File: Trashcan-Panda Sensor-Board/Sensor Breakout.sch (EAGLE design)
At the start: 14 parts, among them J6 BM06B-SRSS-TBT(LF)(SN), U2 VL53L1X

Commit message: Rectangular Sensor Board
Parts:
- removed C1: 4.7uF, SparkFun-Capacitors:4.7UF0603
- removed JP3, JP4: STAND-OFF, SparkFun:STAND-OFF
- removed R1: 10k, SparkFun-Resistors:10KOHM-0603-1/10W-1%
- added C3: (no value), Custom Components:CAP-MF-10UF-1206
- added Q1: BSS215P, Custom Components:BSS215P
- added R4: 100k, Custom Components:RESISTOR-MF-100K-0805
- added U1: LIS3DH, Custom Components:LIS3DH
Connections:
- removed net !INT: J6.5, R1.1, U2.!INT
- new net !EN: J6.6, Q1.GATE, R4.1
- new net INT: J6.5, U1.INT1
- new net VCC-IN: J6.2, Q1.SOURCE, R4.2
- net !SHUT: no longer J6.6
- net GND: now also C3.P$2, U1.GND, U1.GND1; no longer C1.2
- net SCL: now also U1.SCL/SPC
- net SDA: now also U1.SDA/SDI/SDO
- net VCC: now also C3.P$1, Q1.DRAIN, U1.VDD, U1.VDD_IO; no longer C1.1, J6.2, R1.2

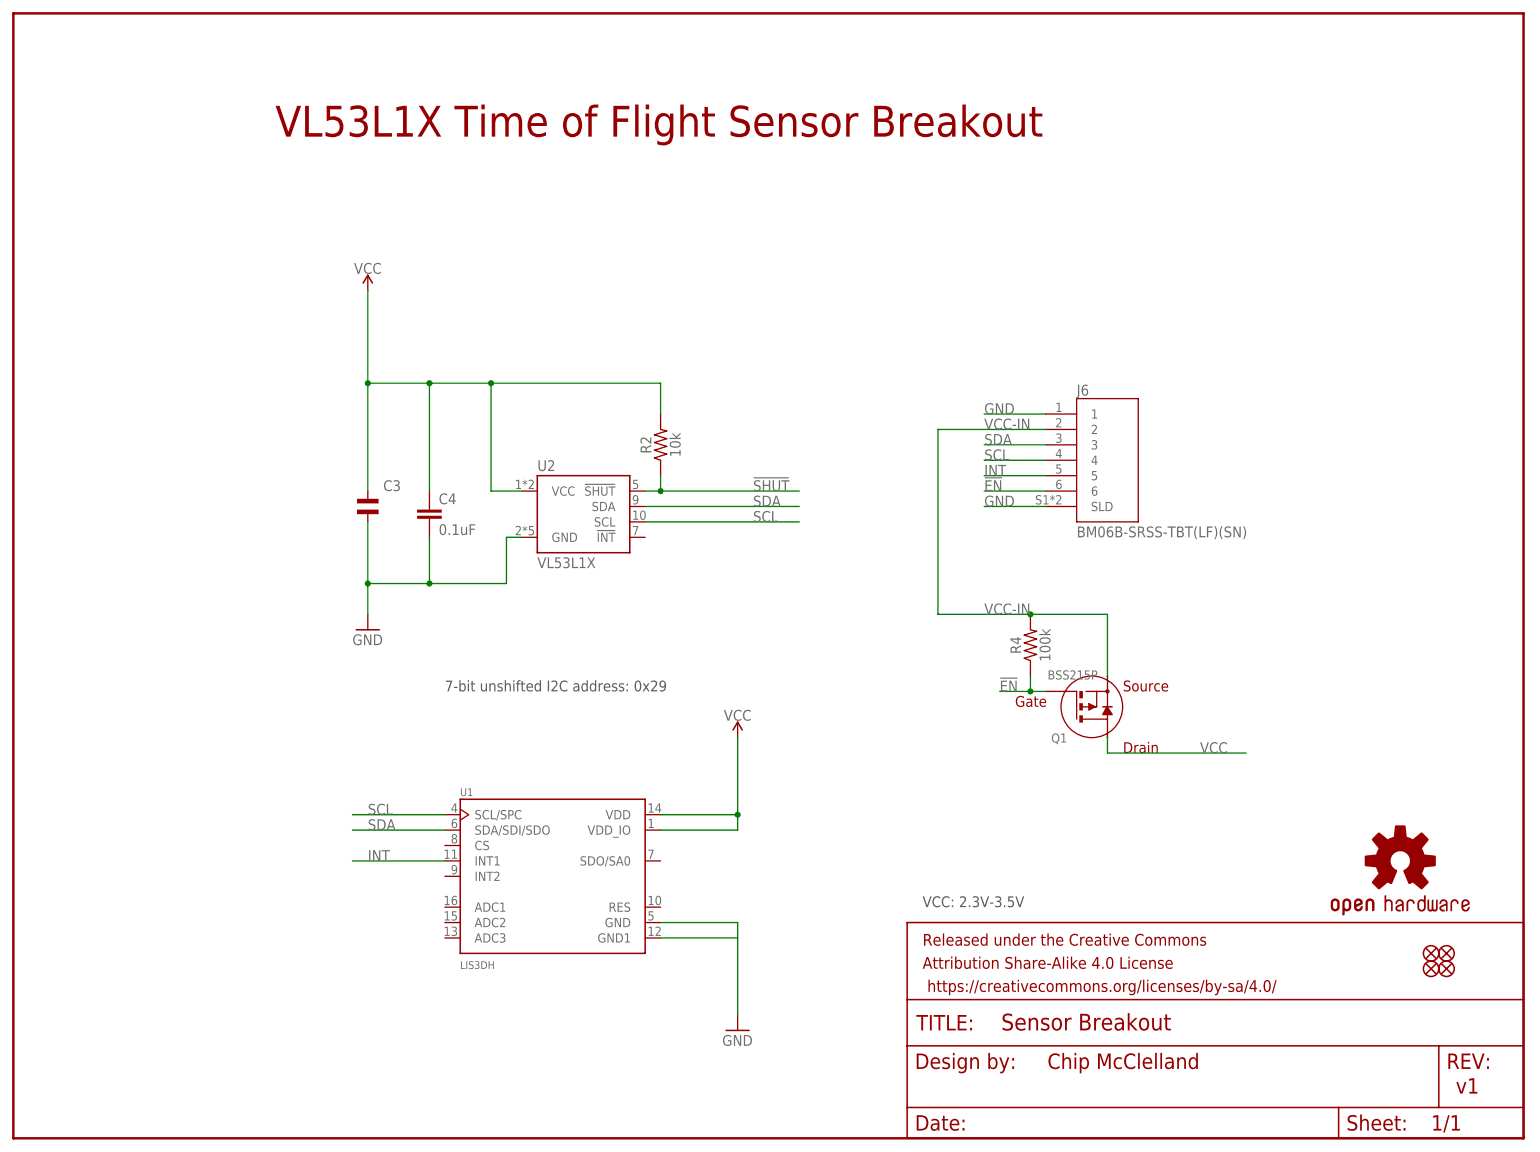
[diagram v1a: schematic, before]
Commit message: Updated battery board to v1.1
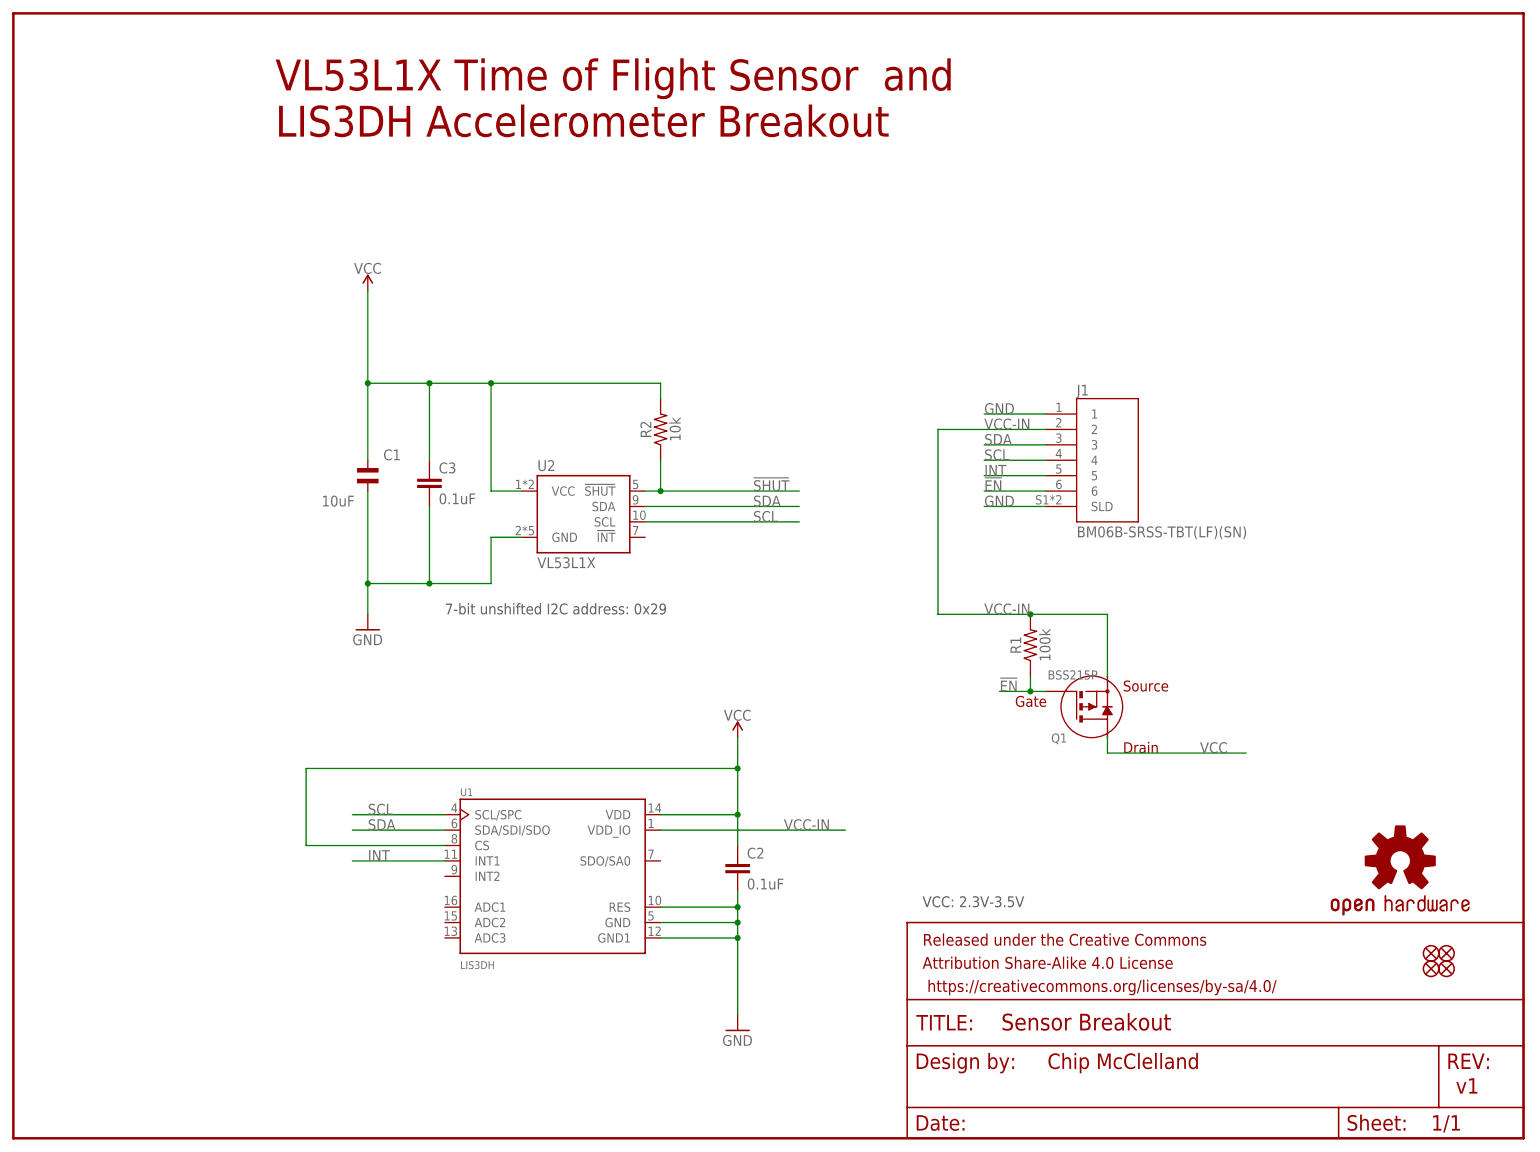
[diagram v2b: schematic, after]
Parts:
- removed C4: 0.1uF, SparkFun-Capacitors:0.1UF-0603-25V-(+80/-20%)
- added C1: 10uF, Custom Components:CAP-MF-10UF-1206
- added C2: 0.1uF, SparkFun-Capacitors:0.1UF-0603-25V-(+80/-20%)
- C3: value (none) -> 0.1uF; device Custom Components:CAP-MF-10UF-1206 -> SparkFun-Capacitors:0.1UF-0603-25V-(+80/-20%)
- renumbered J6 to J1, R4 to R1
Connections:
- net GND: now also C1.P$2, C2.2, C3.2, U1.RES; no longer C3.P$2, C4.2
- net VCC: now also C1.P$1, C2.1, C3.1, U1.CS; no longer C3.P$1, C4.1, U1.VDD_IO
- net VCC-IN: now also U1.VDD_IO
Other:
- note added: "VL53L1X Time of Flight Sensor and LIS3DH Accelerometer Breakout"
- note removed: "VL53L1X Time of Flight Sensor Breakout"
- moved on the sheet: R2

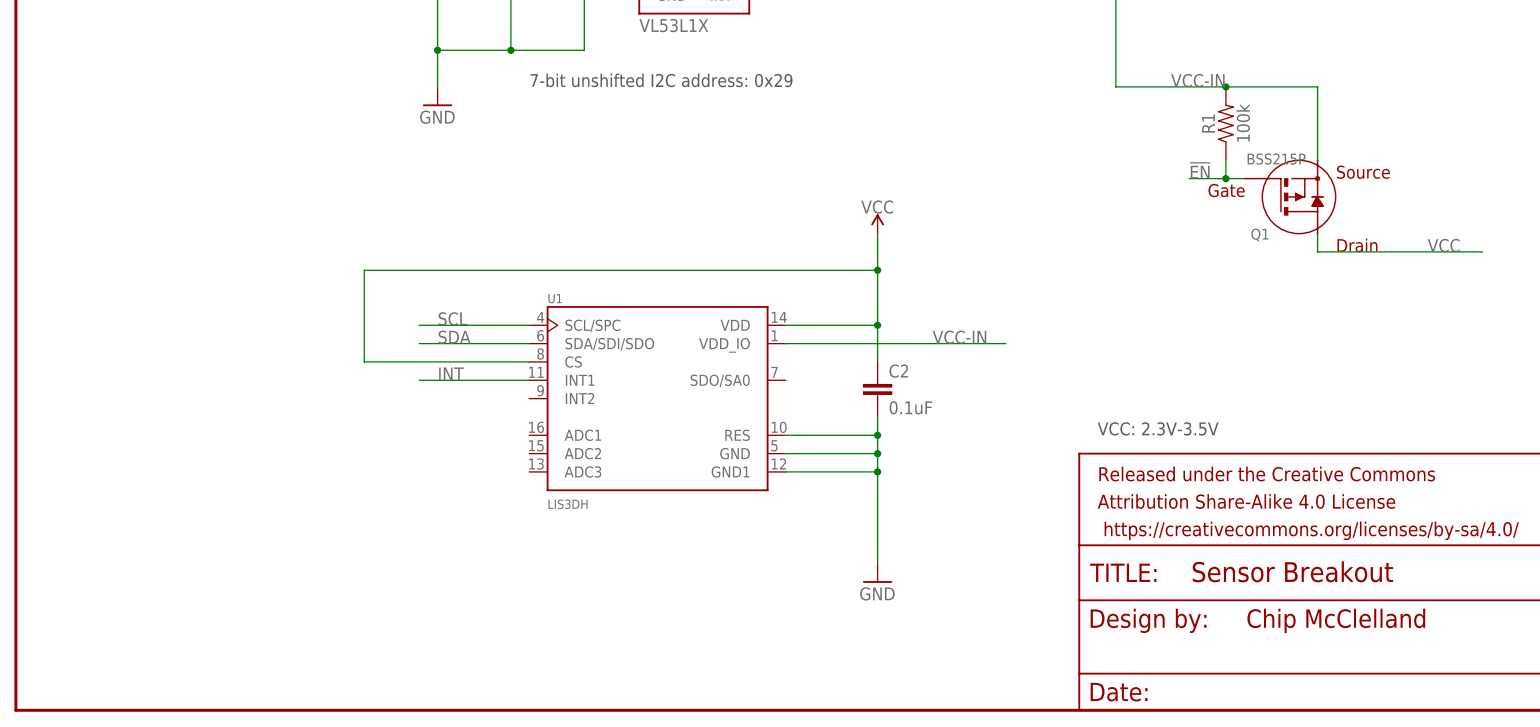
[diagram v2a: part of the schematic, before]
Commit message: Updated - Grounded address pin
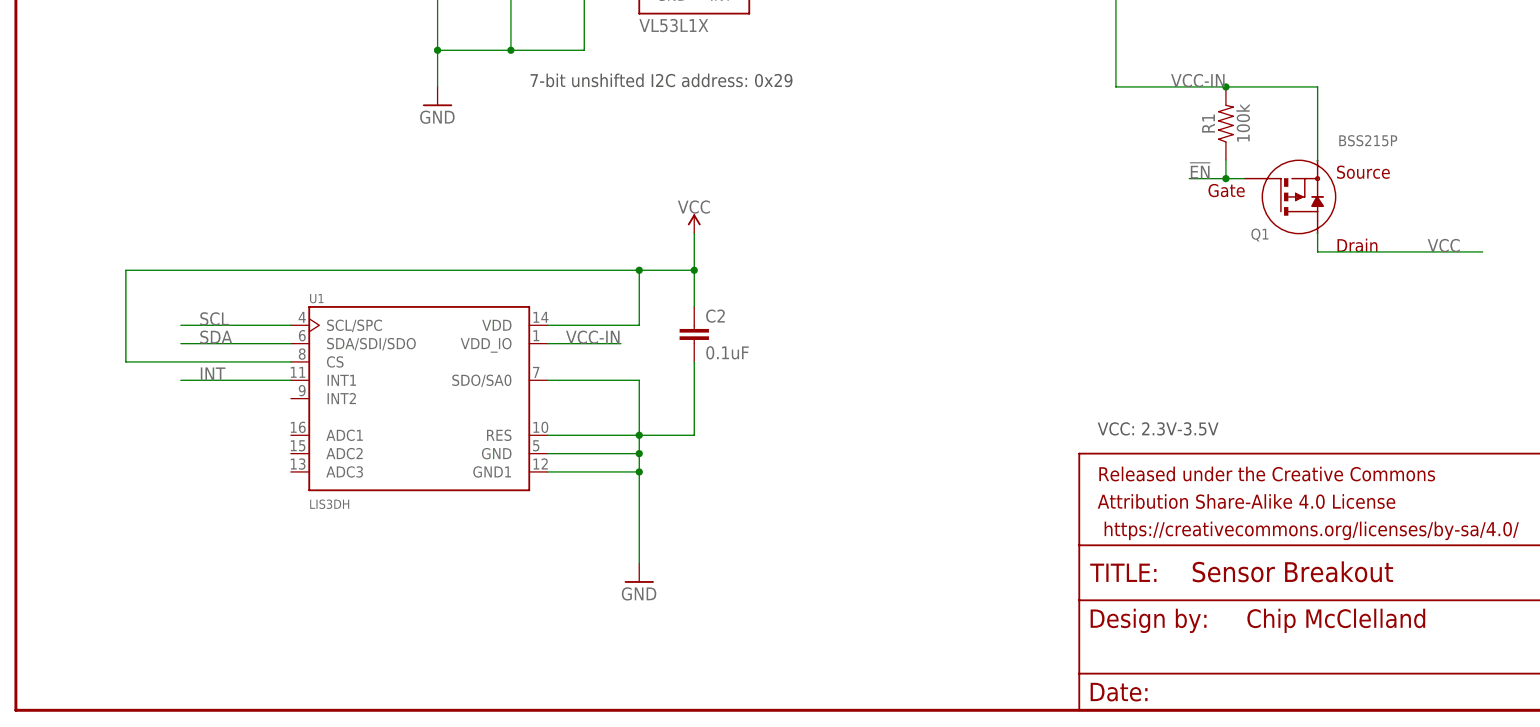
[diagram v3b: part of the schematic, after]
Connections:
- net GND: now also U1.SDO/SA0
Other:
- moved on the sheet: C2, U1
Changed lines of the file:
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@@
 <attribute name="VALUE" x="175.26" y="99.06" size="1.778" layer="96"/>
 </instance>
-<instance part="U1" gate="G$1" x="88.9" y="43.18" smashed="yes">
-<attribute name="NAME" x="73.6364" y="56.4085" size="1.27196875" layer="95"/>
-<attribute name="VALUE" x="73.6323" y="27.9123" size="1.272309375" layer="96"/>
-</instance>
-<instance part="SUPPLY1" gate="G$1" x="119.38" y="66.04" smashed="yes">
-<attribute name="VALUE" x="119.38" y="68.834" size="1.778" layer="96" align="bottom-center"/>
-</instance>
-<instance part="GND1" gate="1" x="119.38" y="17.78" smashed="yes">
-<attribute name="VALUE" x="116.84" y="15.24" size="1.778" layer="96"/>
+<instance part="U1" gate="G$1" x="55.88" y="43.18" smashed="yes">
+<attribute name="NAME" x="40.6164" y="56.4085" size="1.27196875" layer="95"/>
+<attribute name="VALUE" x="40.6123" y="27.9123" size="1.272309375" layer="96"/>
+</instance>
+<instance part="SUPPLY1" gate="G$1" x="93.98" y="66.04" smashed="yes">
+<attribute name="VALUE" x="93.98" y="68.834" size="1.778" layer="96" align="bottom-center"/>
+</instance>
+<instance part="GND1" gate="1" x="86.36" y="17.78" smashed="yes">
+<attribute name="VALUE" x="83.82" y="15.24" size="1.778" layer="96"/>
 </instance>
 <instance part="SUPPLY2" gate="G$1" x="58.42" y="139.7" smashed="yes">
@@
 </instance>
 <instance part="Q1" gate="G$1" x="177.8" y="71.12" smashed="yes">
-<attribute name="VALUE" x="170.46" y="77.12" size="1.5" layer="96" ratio="0" rot="MR180"/>
+<attribute name="VALUE" x="183.16" y="79.66" size="1.5" layer="96" ratio="0" rot="MR180"/>
 <attribute name="NAME" x="171.06" y="66.72" size="1.5" layer="95" ratio="0" rot="MR180"/>
 </instance>
-<instance part="C2" gate="G$1" x="119.38" y="43.18" smashed="yes">
-<attribute name="NAME" x="120.904" y="46.101" size="1.778" layer="95" font="vector"/>
-<attribute name="VALUE" x="120.904" y="41.021" size="1.778" layer="96" font="vector"/>
+<instance part="C2" gate="G$1" x="93.98" y="50.8" smashed="yes">
+<attribute name="NAME" x="95.504" y="53.721" size="1.778" layer="95" font="vector"/>
+<attribute name="VALUE" x="95.504" y="48.641" size="1.778" layer="96" font="vector"/>
 </instance>
 </instances>
@@
 <pinref part="GND1" gate="1" pin="GND"/>
 <pinref part="U1" gate="G$1" pin="GND"/>
-<wire x1="119.38" y1="35.56" x2="119.38" y2="33.02" width="0.1524" layer="91"/>
-<wire x1="119.38" y1="33.02" x2="119.38" y2="20.32" width="0.1524" layer="91"/>
-<wire x1="106.68" y1="35.56" x2="119.38" y2="35.56" width="0.1524" layer="91"/>
+<wire x1="86.36" y1="35.56" x2="86.36" y2="33.02" width="0.1524" layer="91"/>
+<wire x1="86.36" y1="33.02" x2="86.36" y2="20.32" width="0.1524" layer="91"/>
+<wire x1="73.66" y1="35.56" x2="86.36" y2="35.56" width="0.1524" layer="91"/>
 <pinref part="C2" gate="G$1" pin="2"/>
-<wire x1="119.38" y1="40.64" x2="119.38" y2="38.1" width="0.1524" layer="91"/>
-<junction x="119.38" y="35.56"/>
+<junction x="86.36" y="35.56"/>
 <pinref part="U1" gate="G$1" pin="RES"/>
-<wire x1="119.38" y1="38.1" x2="119.38" y2="35.56" width="0.1524" layer="91"/>
-<wire x1="106.68" y1="38.1" x2="119.38" y2="38.1" width="0.1524" layer="91"/>
-<junction x="119.38" y="38.1"/>
+<wire x1="86.36" y1="38.1" x2="86.36" y2="35.56" width="0.1524" layer="91"/>
+<wire x1="73.66" y1="38.1" x2="86.36" y2="38.1" width="0.1524" layer="91"/>
+<junction x="86.36" y="38.1"/>
 <pinref part="U1" gate="G$1" pin="GND1"/>
-<wire x1="106.68" y1="33.02" x2="119.38" y2="33.02" width="0.1524" layer="91"/>
-<junction x="119.38" y="33.02"/>
+<wire x1="73.66" y1="33.02" x2="86.36" y2="33.02" width="0.1524" layer="91"/>
+<junction x="86.36" y="33.02"/>
+<pinref part="U1" gate="G$1" pin="SDO/SA0"/>
+<wire x1="73.66" y1="45.72" x2="86.36" y2="45.72" width="0.1524" layer="91"/>
+<wire x1="86.36" y1="45.72" x2="86.36" y2="38.1" width="0.1524" layer="91"/>
+<wire x1="86.36" y1="38.1" x2="93.98" y2="38.1" width="0.1524" layer="91"/>
+<wire x1="93.98" y1="38.1" x2="93.98" y2="48.26" width="0.1524" layer="91"/>
 </segment>
 </net>
@@
 <segment>
 <pinref part="U1" gate="G$1" pin="SCL/SPC"/>
-<wire x1="71.12" y1="53.34" x2="55.88" y2="53.34" width="0.1524" layer="91"/>
-<label x="58.42" y="53.34" size="1.778" layer="95"/>
+<wire x1="38.1" y1="53.34" x2="22.86" y2="53.34" width="0.1524" layer="91"/>
+<label x="25.4" y="53.34" size="1.778" layer="95"/>
 </segment>
 </net>
@@
 <segment>
 <pinref part="U1" gate="G$1" pin="SDA/SDI/SDO"/>
-<wire x1="71.12" y1="50.8" x2="55.88" y2="50.8" width="0.1524" layer="91"/>
-<label x="58.42" y="50.8" size="1.778" layer="95"/>
+<wire x1="38.1" y1="50.8" x2="22.86" y2="50.8" width="0.1524" layer="91"/>
+<label x="25.4" y="50.8" size="1.778" layer="95"/>
 </segment>
 </net>
@@
 <pinref part="U1" gate="G$1" pin="VDD"/>
 <pinref part="SUPPLY1" gate="G$1" pin="VCC"/>
-<wire x1="106.68" y1="53.34" x2="119.38" y2="53.34" width="0.1524" layer="91"/>
-<wire x1="119.38" y1="53.34" x2="119.38" y2="60.96" width="0.1524" layer="91"/>
-<wire x1="119.38" y1="60.96" x2="119.38" y2="66.04" width="0.1524" layer="91"/>
-<junction x="119.38" y="53.34"/>
+<wire x1="73.66" y1="53.34" x2="86.36" y2="53.34" width="0.1524" layer="91"/>
+<wire x1="86.36" y1="53.34" x2="86.36" y2="60.96" width="0.1524" layer="91"/>
 <pinref part="C2" gate="G$1" pin="1"/>
-<wire x1="119.38" y1="48.26" x2="119.38" y2="53.34" width="0.1524" layer="91"/>
 <pinref part="U1" gate="G$1" pin="CS"/>
-<wire x1="71.12" y1="48.26" x2="48.26" y2="48.26" width="0.1524" layer="91"/>
-<wire x1="48.26" y1="48.26" x2="48.26" y2="60.96" width="0.1524" layer="91"/>
-<wire x1="48.26" y1="60.96" x2="119.38" y2="60.96" width="0.1524" layer="91"/>
-<junction x="119.38" y="60.96"/>
+<wire x1="38.1" y1="48.26" x2="15.24" y2="48.26" width="0.1524" layer="91"/>
+<wire x1="15.24" y1="48.26" x2="15.24" y2="60.96" width="0.1524" layer="91"/>
+<wire x1="15.24" y1="60.96" x2="86.36" y2="60.96" width="0.1524" layer="91"/>
+<junction x="86.36" y="60.96"/>
+<wire x1="86.36" y1="60.96" x2="93.98" y2="60.96" width="0.1524" layer="91"/>
+<wire x1="93.98" y1="60.96" x2="93.98" y2="55.88" width="0.1524" layer="91"/>
+<wire x1="93.98" y1="66.04" x2="93.98" y2="60.96" width="0.1524" layer="91"/>
+<junction x="93.98" y="60.96"/>
 </segment>
 <segment>
@@
 <segment>
 <pinref part="U1" gate="G$1" pin="INT1"/>
-<wire x1="71.12" y1="45.72" x2="55.88" y2="45.72" width="0.1524" layer="91"/>
-<label x="58.42" y="45.72" size="1.778" layer="95"/>
+<wire x1="38.1" y1="45.72" x2="22.86" y2="45.72" width="0.1524" layer="91"/>
+<label x="25.4" y="45.72" size="1.778" layer="95"/>
 </segment>
 <segment>
@@
 <segment>
 <pinref part="U1" gate="G$1" pin="VDD_IO"/>
-<wire x1="106.68" y1="50.8" x2="137.16" y2="50.8" width="0.1524" layer="91"/>
-<label x="127" y="50.8" size="1.778" layer="95"/>
-</segment>
-</net>
+<wire x1="73.66" y1="50.8" x2="83.82" y2="50.8" width="0.1524" layer="91"/>
+<label x="76.2" y="50.8" size="1.778" layer="95"/>
+</segment>
+</net>
